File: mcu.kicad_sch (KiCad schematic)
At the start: 22 parts, among them U1 STM32H7A3VITx, Y1 ECS-80-10-30B-CWN-TR

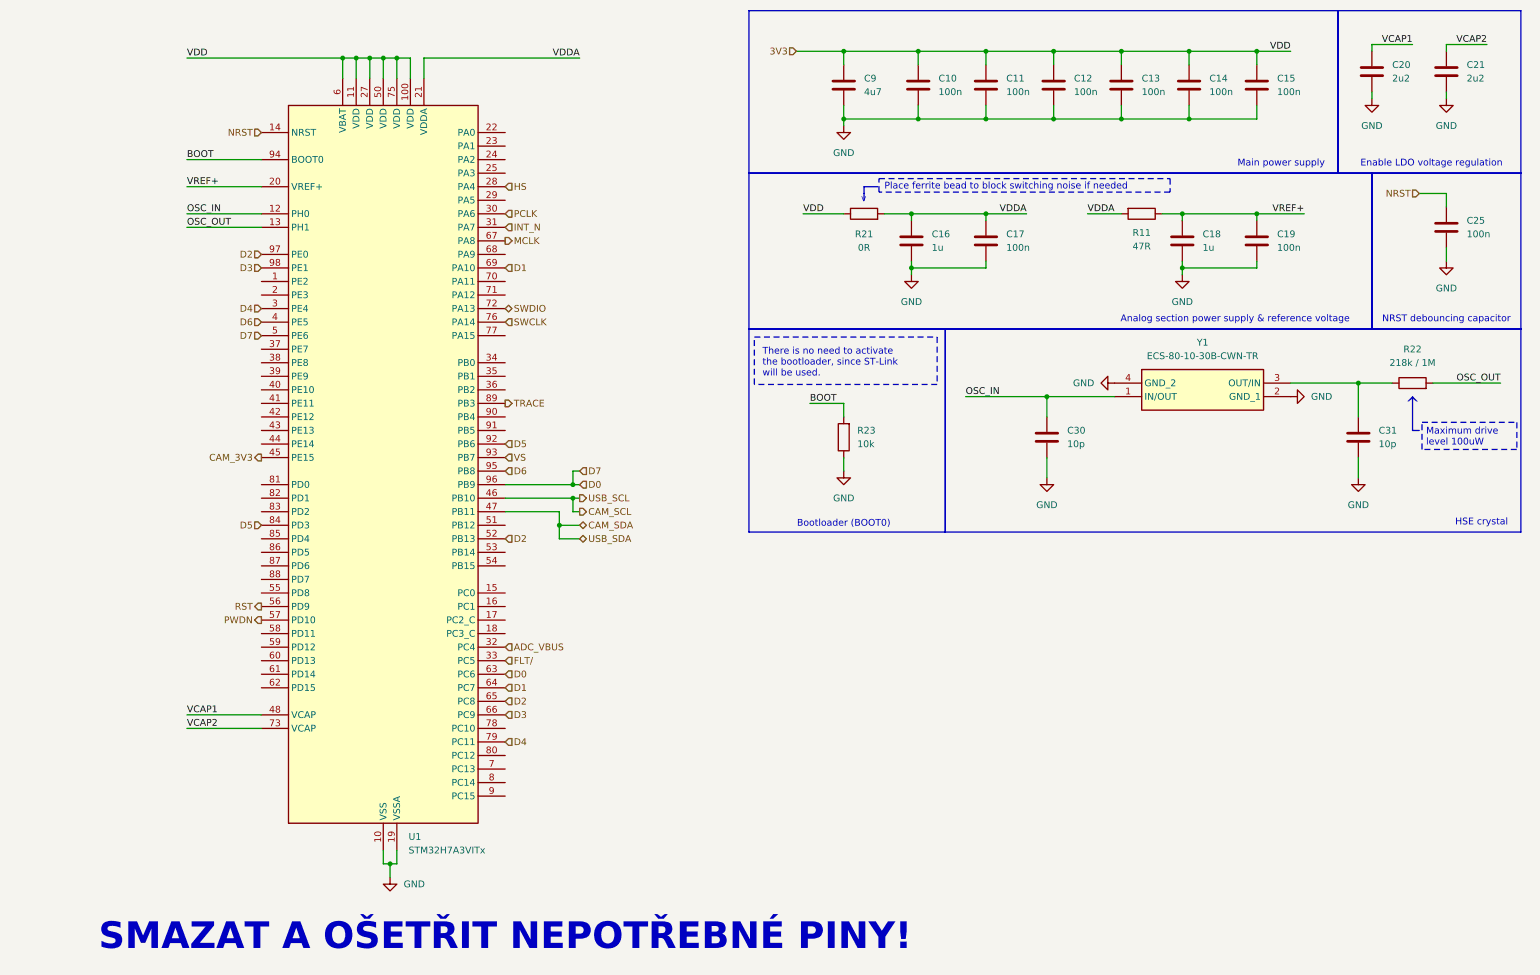
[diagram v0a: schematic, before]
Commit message: USB-B micro added
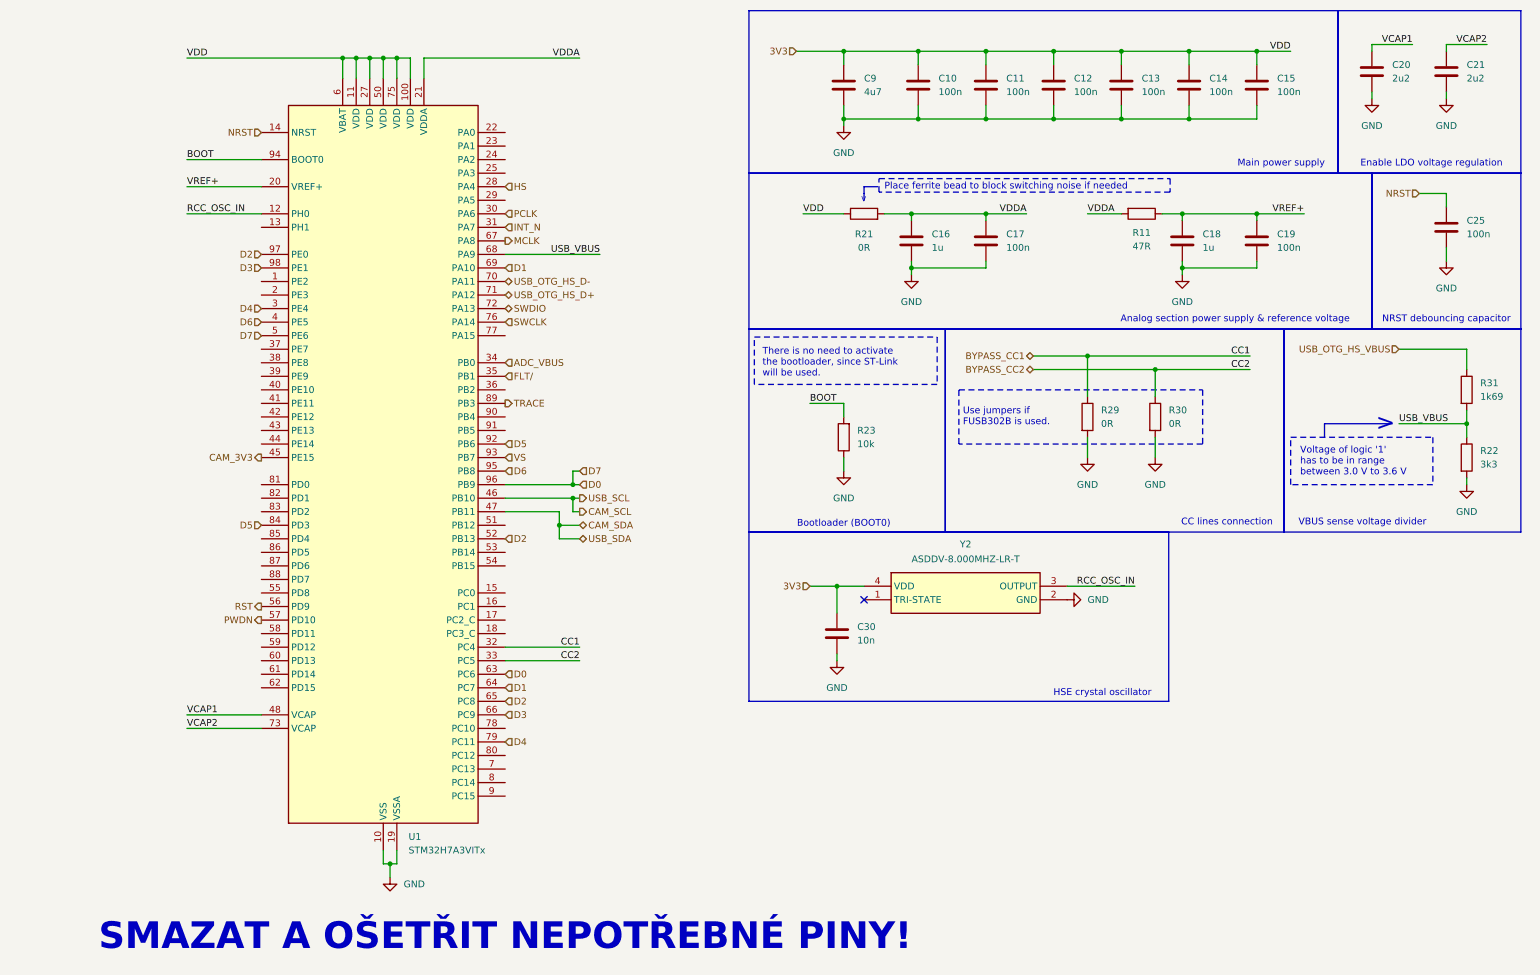
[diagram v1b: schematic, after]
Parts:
- removed C31: 10p, Capacitor_SMD:C_0402_1005Metric, symbol Device:C
- removed Y1: ECS-80-10-30B-CWN-TR, SamacSys_Parts:ECS801830BAGNTR, symbol SamacSys_Parts:ECS-80-10-30B-CWN-TR
- added R29, R30: 0R, Resistor_SMD:R_0402_1005Metric, symbol Device:R
- added R31: 1k69, Resistor_SMD:R_0402_1005Metric, symbol Device:R
- added Y2: ASDDV-8.000MHZ-LR-T, AbraconASDDV, symbol SamacSys_Parts:ASDDV-8.000MHZ-LR-T
- C30: value 10p -> 10n
- R22: value 218k / 1M -> 3k3; footprint Resistor_SMD:R_0603_1608Metric -> Resistor_SMD:R_0402_1005Metric
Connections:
- net 3V3: now also C30.1, Y2.4 (VDD)
- net ADC_VBUS: now also U1.34 (PB0); no longer U1.32 (PC4)
- net FLT/: now also U1.35 (PB1); no longer U1.33 (PC5)
- net GND: now also R22.2, R29.2, R30.2, Y2.2 (GND)
- net USB_VBUS: now reaches R22.1
- net USB_VBUS: now also U1.68 (PA9), R31.2
- net USB_OTG_HS_D-: now reaches U1.70 (PA11)
- net USB_OTG_HS_D+: now reaches U1.71 (PA12)
- net OSC_IN renamed RCC_OSC_IN
- net RCC_OSC_IN: now also Y2.3 (OUTPUT); no longer C30.1
- net OSC_OUT: no longer names the net of U1.13 (PH1)
- net OSC_OUT: no longer R22.2
- new net BYPASS_CC1: R29.1, U1.32 (PC4)
- new net BYPASS_CC2: R30.1, U1.33 (PC5)
- new net USB_OTG_HS_VBUS: R31.1
- no-connect marks 0 -> 1
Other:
- note added: ">"
- note added: "CC lines connection"
- note added: "HSE crystal oscillator"
- note added: "Use jumpers if FUSB302B is used."
- note added: "VBUS sense voltage divider"
- note added: "Voltage of logic '1' has to be in range between 3.0 V to 3.6 V"
- note removed: "HSE crystal"
- note removed: "Maximum drive level 100uW"
- note removed: "^"
